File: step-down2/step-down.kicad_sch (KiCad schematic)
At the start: 22 parts, among them IC1 LTC3807EFE#PBF, IC2 IRF7413ZPBF, IC3 IRF7413ZPBF, J1 Screw_Terminal_01x02, J2 Screw_Terminal_01x02

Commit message: fixed mosfet connections
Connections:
- net GND: now also IC3.2 (S_2), IC3.3 (S_3)
- net at C5.2, D2.1 (K), IC1.13 (SW)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: now also IC2.2 (S_2), IC2.3 (S_3)
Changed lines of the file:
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@@
+	)
+	(junction
+		(at 203.2 90.17)
+		(diameter 0)
+		(color 0 0 0 0)
 	)
 	(junction
@@
 	)
 	(junction
+		(at 203.2 92.71)
+		(diameter 0)
+		(color 0 0 0 0)
+	)
+	(junction
+		(at 203.2 71.12)
+		(diameter 0)
+		(color 0 0 0 0)
+	)
+	(junction
 		(at 231.14 110.49)
 		(diameter 0)
@@
 	(junction
 		(at 163.83 82.55)
+		(diameter 0)
+		(color 0 0 0 0)
+	)
+	(junction
+		(at 203.2 68.58)
 		(diameter 0)
 		(color 0 0 0 0)
@@
 	(wire
 		(pts
+			(xy 203.2 90.17) (xy 203.2 92.71)
+		)
+		(stroke
+			(width 0)
+			(type default)
+		)
+	)
+	(wire
+		(pts
 			(xy 233.68 97.79) (xy 233.68 101.6)
 		)
@@
 		)
 		(stroke
+			(width 0)
+			(type default)
+		)
+	)
+	(wire
+		(pts
+			(xy 203.2 68.58) (xy 203.2 71.12)
+		)
+		(stroke

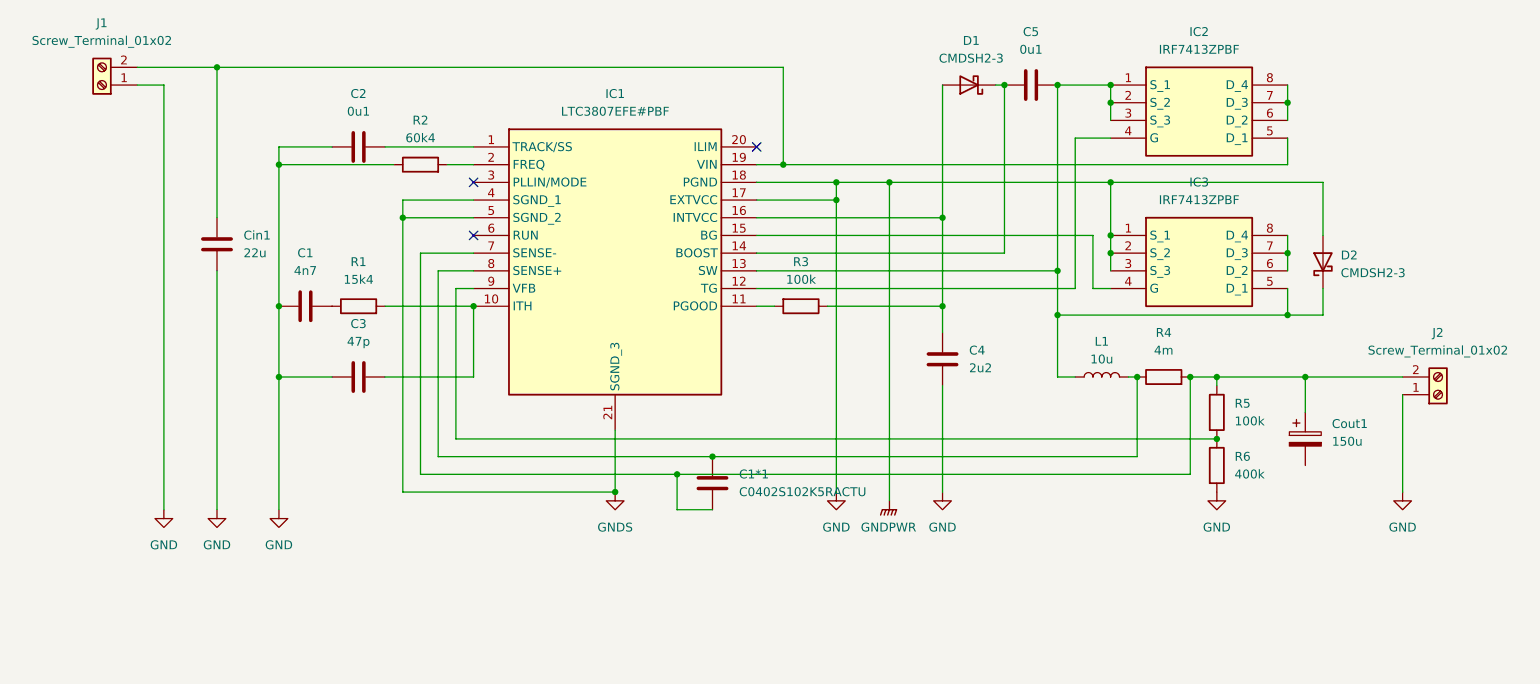
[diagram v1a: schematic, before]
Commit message: fixed mosfet connections
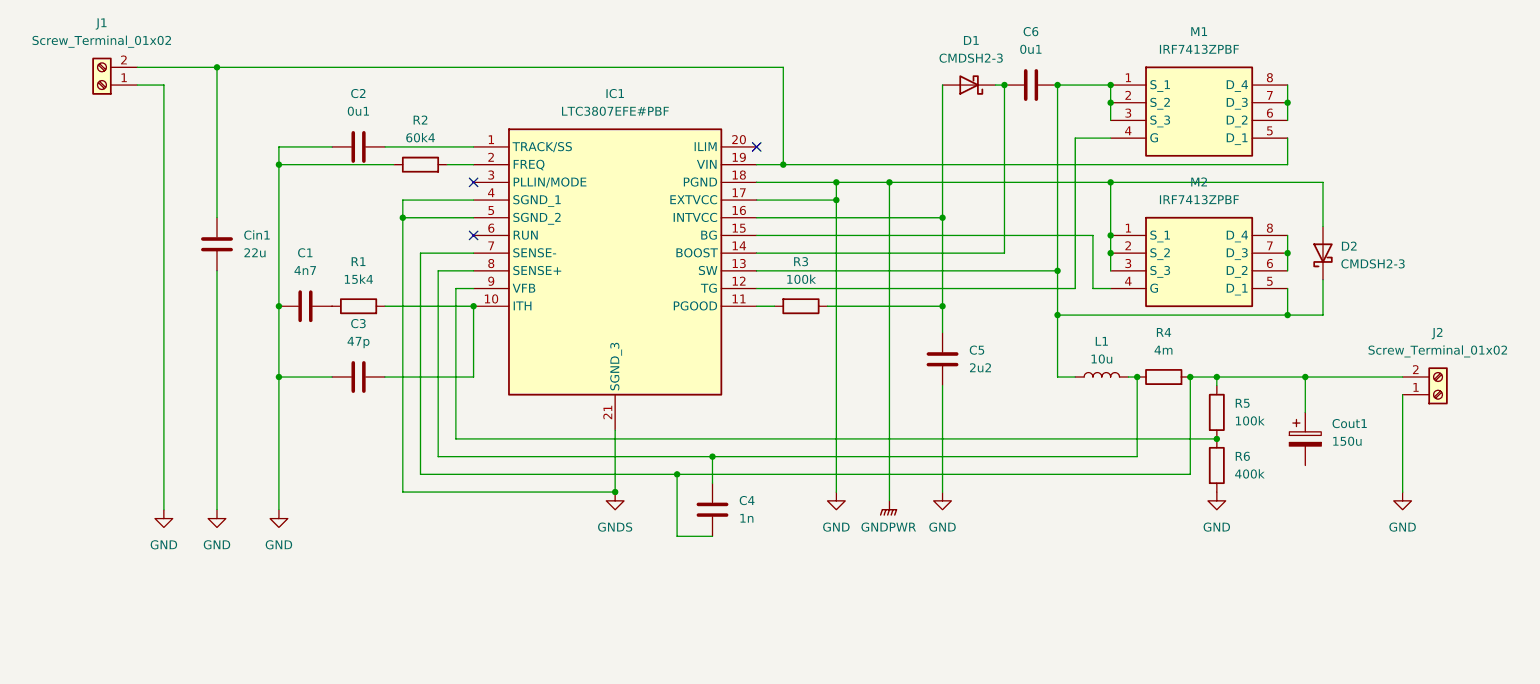
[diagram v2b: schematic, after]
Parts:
- C4: renamed from C1*1; value C0402S102K5RACTU -> 1n
- renumbered C4 to C5, C5 to C6, IC2 to M1, IC3 to M2
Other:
- moved on the sheet: C4, D2
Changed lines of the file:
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@@
 	(wire
 		(pts
-			(xy 140.97 124.46) (xy 140.97 129.54)
+			(xy 140.97 124.46) (xy 140.97 133.35)
 		)
 		(stroke
@@
 	(wire
 		(pts
-			(xy 233.68 82.55) (xy 233.68 90.17)
+			(xy 233.68 82.55) (xy 233.68 88.9)
 		)
 		(stroke
@@
 	(wire
 		(pts
+			(xy 146.05 125.73) (xy 146.05 121.92)
+		)
+		(stroke
+			(width 0)
+			(type default)
+		)
+	)
+	(wire
+		(pts
 			(xy 203.2 82.55) (xy 203.2 90.17)
 		)
@@
 	(wire
 		(pts
-			(xy 233.68 97.79) (xy 233.68 101.6)
+			(xy 233.68 96.52) (xy 233.68 101.6)
 		)
 		(stroke
@@
 	(wire
 		(pts
-			(xy 140.97 129.54) (xy 146.05 129.54)
+			(xy 140.97 133.35) (xy 146.05 133.35)
 		)
 		(stroke
@@
 	(symbol
 		(lib_id "Device:C")
-		(at 146.05 125.73 0)
+		(at 146.05 129.54 0)
 		(unit 1)
 		(exclude_from_sim no)
@@
 		(dnp no)
 		(fields_autoplaced yes)
-		(property "Reference" "C1*1"
-			(at 149.86 124.4599 0)
+		(property "Reference" "C4"
+			(at 149.86 128.2699 0)
 			(effects
 				(font
@@
 			)
 		)
-		(property "Value" "C0402S102K5RACTU"
-			(at 149.86 126.9999 0)
+		(property "Value" "1n"
+			(at 149.86 130.8099 0)
 			(effects
 				(font
@@
 		)
 		(property "Footprint" "C0402"
-			(at 147.0152 129.54 0)
+			(at 147.0152 133.35 0)
 			(effects
 				(font
@@
 		)
 		(property "Datasheet" "~"
-			(at 146.05 125.73 0)
+			(at 146.05 129.54 0)
 			(effects
 				(font
@@
 		)
 		(property "Description" "Unpolarized capacitor"
-			(at 146.05 125.73 0)
+			(at 146.05 129.54 0)
 			(effects
 				(font
@@
 		)
 		(property "Height" "0.55"
-			(at 154.94 521.92 0)
+			(at 154.94 525.73 0)
 			(effects
 				(font
@@
 		)
 		(property "Mouser Part Number" "80-C0402S102K5R"
-			(at 154.94 621.92 0)
+			(at 154.94 625.73 0)
 			(effects
 				(font
@@
 		)
 		(property "Mouser Price/Stock" "https://www.mouser.co.uk/ProductDetail/KEMET/C0402S102K5RACTU?qs=CV4an4nnCD1z917c3mAHAQ%3D%3D"
-			(at 154.94 721.92 0)
+			(at 154.94 725.73 0)
 			(effects
 				(font
@@
 		)
 		(property "Manufacturer_Name" "KEMET"
-			(at 154.94 821.92 0)
+			(at 154.94 825.73 0)
 			(effects
 				(font
@@
 		)
 		(property "Manufacturer_Part_Number" "C0402S102K5RACTU"
-			(at 154.94 921.92 0)
+			(at 154.94 925.73 0)
 			(effects
 				(font
@@
 			(project "step-down"
 				(path "/270a0c1d-99e0-47c8-a788-488ffbf33d34"
-					(reference "C1*1")
+					(reference "C4")
 					(unit 1)
 				)
@@
 		(dnp no)
 		(fields_autoplaced yes)
-		(property "Reference" "IC3"
+		(property "Reference" "M2"
 			(at 215.9 82.55 0)
 			(effects
@@
 			(project "step-down"
 				(path "/270a0c1d-99e0-47c8-a788-488ffbf33d34"
-					(reference "IC3")
+					(reference "M2")
 					(unit 1)
 				)
@@
 		(dnp no)
 		(fields_autoplaced yes)
-		(property "Reference" "C5"
+		(property "Reference" "C6"
 			(at 191.77 60.96 90)
 			(effects
@@
 			(project ""
 				(path "/270a0c1d-99e0-47c8-a788-488ffbf33d34"
-					(reference "C5")
+					(reference "C6")
 					(unit 1)
 				)
@@
 		(dnp no)
 		(fields_autoplaced yes)
-		(property "Reference" "IC2"
+		(property "Reference" "M1"
 			(at 215.9 60.96 0)
 			(effects
@@
 			(project ""
 				(path "/270a0c1d-99e0-47c8-a788-488ffbf33d34"
-					(reference "IC2")
+					(reference "M1")
 					(unit 1)
 				)
@@
 	(symbol
 		(lib_id "Device:D_Schottky")
-		(at 233.68 93.98 90)
+		(at 233.68 92.71 90)
 		(unit 1)
 		(exclude_from_sim no)
@@
 		(fields_autoplaced yes)
 		(property "Reference" "D2"
-			(at 236.22 93.0274 90)
+			(at 236.22 91.7574 90)
 			(effects
 				(font
@@
 		)
 		(property "Value" "CMDSH2-3"
-			(at 236.22 95.5674 90)
+			(at 236.22 94.2974 90)
 			(effects
 				(font
@@
 		)
 		(property "Footprint" "footprints:CMDSH2-3_TR_PBFREE"
-			(at 233.68 93.98 0)
+			(at 233.68 92.71 0)
 			(effects
 				(font
@@
 		)
 		(property "Datasheet" "~"
-			(at 233.68 93.98 0)
+			(at 233.68 92.71 0)
 			(effects
 				(font
@@
 		)
 		(property "Description" "Schottky diode"
-			(at 233.68 93.98 0)
+			(at 233.68 92.71 0)
 			(effects
 				(font
@@
 		(dnp no)
 		(fields_autoplaced yes)
-		(property "Reference" "C4"
+		(property "Reference" "C5"
 			(at 182.88 106.6799 0)
 			(effects
@@
 			(project ""
 				(path "/270a0c1d-99e0-47c8-a788-488ffbf33d34"
-					(reference "C4")
+					(reference "C5")
 					(unit 1)
 				)

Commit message: gnd fix
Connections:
- net GND: now also Cout1.2
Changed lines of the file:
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@@
+	(wire
+		(pts
+			(xy 231.14 123.19) (xy 231.14 127)
+		)
+		(stroke
+			(width 0)
+			(type default)
+		)
+	)
 	(wire
 		(pts
@@
 					(unit 1)
 				)
+			)
+		)
+	)
+	(symbol
+		(lib_id "power:GND")
+		(at 231.14 127 0)
+		(unit 1)
+		(exclude_from_sim no)
+		(in_bom yes)
+		(on_board yes)
+		(dnp no)
+		(fields_autoplaced yes)
+		(property "Reference" "#PWR010"
+			(at 231.14 133.35 0)
+			(effects
+				(font
+					(size 1.27 1.27)
+				)
+				(hide yes)
+			)
+		)
+		(property "Value" "GND"
+			(at 231.14 132.08 0)
+			(effects
+				(font
+					(size 1.27 1.27)
+				)
+			)
+		)
+		(property "Footprint" ""
+			(at 231.14 127 0)
+			(effects
+				(font
+					(size 1.27 1.27)
+				)
+				(hide yes)
+			)
+		)
+		(property "Datasheet" ""
+			(at 231.14 127 0)
+			(effects
+				(font
+					(size 1.27 1.27)
+				)
+				(hide yes)
+			)
+		)
+		(property "Description" "Power symbol creates a global label with name \"GND\" , ground"
+			(at 231.14 127 0)
+			(effects
+				(font
+					(size 1.27 1.27)
+				)
+				(hide yes)
+			)
+		)
+		(pin "1"
+		)
+		(instances
+			(project ""
+				(path "/270a0c1d-99e0-47c8-a788-488ffbf33d34"
+					(reference "#PWR010")
+					(unit 1)
+				)

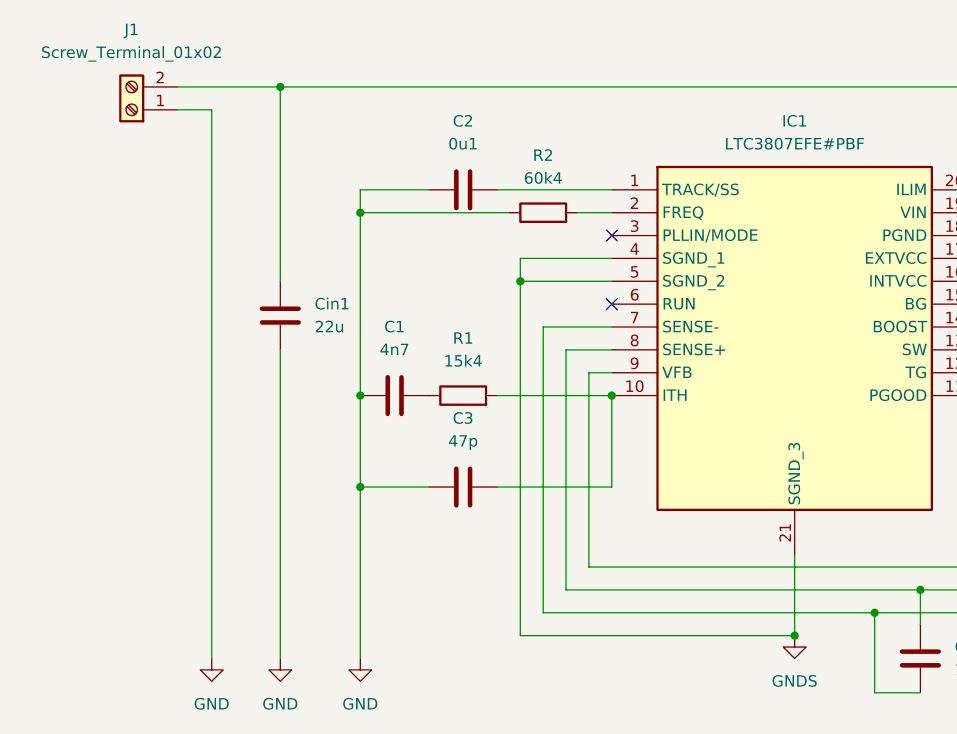
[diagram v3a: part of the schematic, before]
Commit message: fixed ERC error
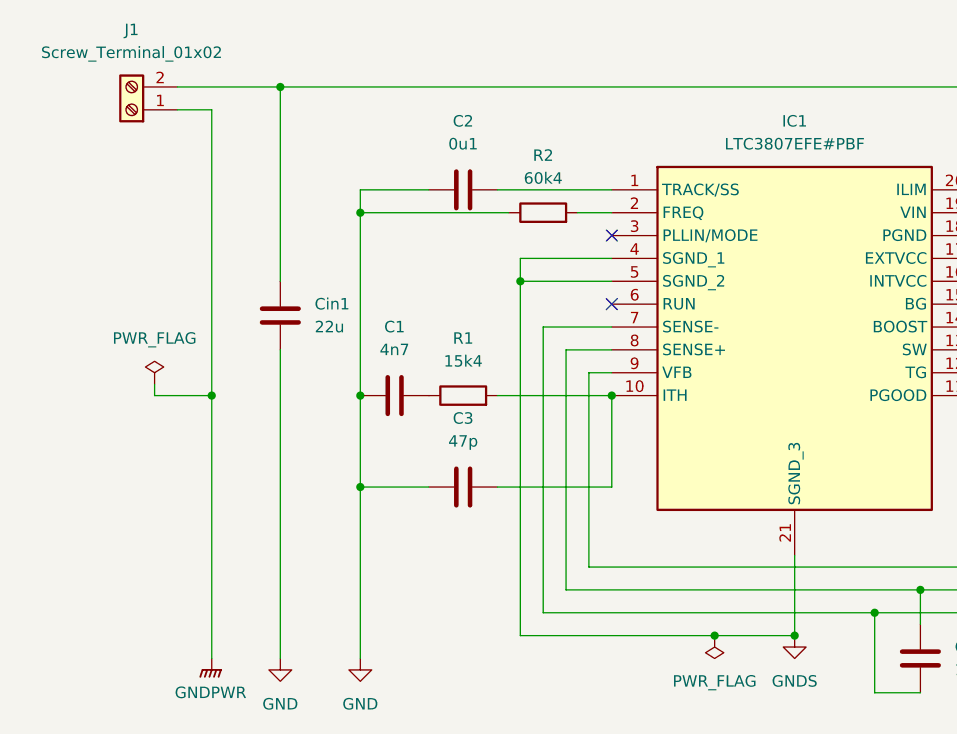
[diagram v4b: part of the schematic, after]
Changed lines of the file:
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@@
 	)
 	(junction
+		(at 67.31 100.33)
+		(diameter 0)
+		(color 0 0 0 0)
+	)
+	(junction
 		(at 179.07 100.33)
 		(diameter 0)
@@
 	)
 	(junction
+		(at 123.19 127)
+		(diameter 0)
+		(color 0 0 0 0)
+	)
+	(junction
 		(at 214.63 110.49)
 		(diameter 0)
@@
 	(wire
 		(pts
+			(xy 67.31 100.33) (xy 67.31 129.54)
+		)
+		(stroke
+			(width 0)
+			(type default)
+		)
+	)
+	(wire
+		(pts
 			(xy 187.96 68.58) (xy 187.96 92.71)
 		)
@@
 	(wire
 		(pts
-			(xy 101.6 127) (xy 132.08 127)
+			(xy 101.6 127) (xy 123.19 127)
 		)
 		(stroke
@@
 	(wire
 		(pts
+			(xy 123.19 127) (xy 132.08 127)
+		)
+		(stroke
+			(width 0)
+			(type default)
+		)
+	)
+	(wire
+		(pts
 			(xy 106.68 121.92) (xy 146.05 121.92)
 		)
@@
 	(wire
 		(pts
+			(xy 60.96 99.06) (xy 60.96 100.33)
+		)
+		(stroke
+			(width 0)
+			(type default)
+		)
+	)
+	(wire
+		(pts
 			(xy 179.07 87.63) (xy 179.07 100.33)
 		)
@@
 	(wire
 		(pts
-			(xy 67.31 68.58) (xy 67.31 129.54)
+			(xy 67.31 68.58) (xy 67.31 100.33)
 		)
 		(stroke
@@
 	(wire
 		(pts
+			(xy 60.96 100.33) (xy 67.31 100.33)
+		)
+		(stroke
+			(width 0)
+			(type default)
+		)
+	)
+	(wire
+		(pts
 			(xy 104.14 124.46) (xy 140.97 124.46)
 		)
@@
 	(symbol
 		(lib_id "power:GND")
-		(at 67.31 129.54 0)
+		(at 231.14 127 0)
 		(unit 1)
 		(exclude_from_sim no)
@@
 		(dnp no)
 		(fields_autoplaced yes)
-		(property "Reference" "#PWR01"
-			(at 67.31 135.89 0)
+		(property "Reference" "#PWR010"
+			(at 231.14 133.35 0)
 			(effects
 				(font
@@
 		)
 		(property "Value" "GND"
-			(at 67.31 134.62 0)
+			(at 231.14 132.08 0)
 			(effects
 				(font
@@
 		)
 		(property "Footprint" ""
-			(at 67.31 129.54 0)
+			(at 231.14 127 0)
 			(effects
 				(font
@@
 		)
 		(property "Datasheet" ""
-			(at 67.31 129.54 0)
+			(at 231.14 127 0)
 			(effects
 				(font
@@
 		)
 		(property "Description" "Power symbol creates a global label with name \"GND\" , ground"
-			(at 67.31 129.54 0)
+			(at 231.14 127 0)
 			(effects
 				(font
@@
 			(project ""
 				(path "/270a0c1d-99e0-47c8-a788-488ffbf33d34"
-					(reference "#PWR01")
+					(reference "#PWR010")
 					(unit 1)
 				)
@@
 	)
 	(symbol
-		(lib_id "power:GND")
-		(at 231.14 127 0)
+		(lib_id "Device:R")
+		(at 104.14 80.01 90)
 		(unit 1)
 		(exclude_from_sim no)
@@
 		(dnp no)
 		(fields_autoplaced yes)
-		(property "Reference" "#PWR010"
-			(at 231.14 133.35 0)
+		(property "Reference" "R2"
+			(at 104.14 73.66 90)
 			(effects
 				(font
 					(size 1.27 1.27)
 				)
-				(hide yes)
 			)
 		)
-		(property "Value" "GND"
-			(at 231.14 132.08 0)
+		(property "Value" "60k4"
+			(at 104.14 76.2 90)
 			(effects
 				(font
@@
 			)
 		)
-		(property "Footprint" ""
-			(at 231.14 127 0)
+		(property "Footprint" "footprints:ERJ-XGNF6042Y"
+			(at 104.14 81.788 90)
 			(effects
 				(font
@@
 			)
 		)
-		(property "Datasheet" ""
-			(at 231.14 127 0)
+		(property "Datasheet" "~"
+			(at 104.14 80.01 0)
 			(effects
 				(font
@@
 			)
 		)
-		(property "Description" "Power symbol creates a global label with name \"GND\" , ground"
-			(at 231.14 127 0)
+		(property "Description" "Resistor"
+			(at 104.14 80.01 0)
 			(effects
 				(font
@@
 		(pin "1"
 		)
+		(pin "2"
+		)
 		(instances
 			(project ""
 				(path "/270a0c1d-99e0-47c8-a788-488ffbf33d34"
-					(reference "#PWR010")
+					(reference "R2")
 					(unit 1)
 				)
@@
 	)
 	(symbol
-		(lib_id "Device:R")
-		(at 104.14 80.01 90)
+		(lib_id "power:PWR_FLAG")
+		(at 123.19 127 180)
 		(unit 1)
 		(exclude_from_sim no)
@@
 		(dnp no)
 		(fields_autoplaced yes)
-		(property "Reference" "R2"
-			(at 104.14 73.66 90)
+		(property "Reference" "#FLG02"
+			(at 123.19 128.905 0)
 			(effects
 				(font
 					(size 1.27 1.27)
 				)
+				(hide yes)
 			)
 		)
-		(property "Value" "60k4"
-			(at 104.14 76.2 90)
+		(property "Value" "PWR_FLAG"
+			(at 123.19 132.08 0)
 			(effects
 				(font
@@
 			)
 		)
-		(property "Footprint" "footprints:ERJ-XGNF6042Y"
-			(at 104.14 81.788 90)
+		(property "Footprint" ""
+			(at 123.19 127 0)
 			(effects
 				(font
@@
 		)
 		(property "Datasheet" "~"
-			(at 104.14 80.01 0)
+			(at 123.19 127 0)
 			(effects
 				(font
@@
 			)
 		)
-		(property "Description" "Resistor"
-			(at 104.14 80.01 0)
+		(property "Description" "Special symbol for telling ERC where power comes from"
+			(at 123.19 127 0)
 			(effects
 				(font
@@
 		(pin "1"
 		)
-		(pin "2"
-		)
 		(instances
 			(project ""
 				(path "/270a0c1d-99e0-47c8-a788-488ffbf33d34"
-					(reference "R2")
+					(reference "#FLG02")
 					(unit 1)
 				)
@@
 					(unit 1)
 				)
+			)
+		)
+	)
+	(symbol
+		(lib_id "power:PWR_FLAG")
+		(at 60.96 99.06 0)
+		(unit 1)
+		(exclude_from_sim no)
+		(in_bom yes)
+		(on_board yes)
+		(dnp no)
+		(fields_autoplaced yes)
+		(property "Reference" "#FLG01"
+			(at 60.96 97.155 0)
+			(effects
+				(font
+					(size 1.27 1.27)
+				)
+				(hide yes)
+			)
+		)
+		(property "Value" "PWR_FLAG"
+			(at 60.96 93.98 0)
+			(effects
+				(font
+					(size 1.27 1.27)
+				)
+			)
+		)
+		(property "Footprint" ""
+			(at 60.96 99.06 0)
+			(effects
+				(font
+					(size 1.27 1.27)
+				)
+				(hide yes)
+			)
+		)
+		(property "Datasheet" "~"
+			(at 60.96 99.06 0)
+			(effects
+				(font
+					(size 1.27 1.27)
+				)
+				(hide yes)
+			)
+		)
+		(property "Description" "Special symbol for telling ERC where power comes from"
+			(at 60.96 99.06 0)
+			(effects
+				(font
+					(size 1.27 1.27)
+				)
+				(hide yes)
+			)
+		)
+		(pin "1"
+		)
+		(instances
+			(project ""
+				(path "/270a0c1d-99e0-47c8-a788-488ffbf33d34"
+					(reference "#FLG01")
+					(unit 1)
+				)
+			)
+		)
+	)
+	(symbol
+		(lib_id "power:GNDPWR")
+		(at 67.31 129.54 0)
+		(unit 1)
+		(exclude_from_sim no)
+		(in_bom yes)
+		(on_board yes)
+		(dnp no)
+		(fields_autoplaced yes)
+		(property "Reference" "#PWR01"
+			(at 67.31 134.62 0)
+			(effects
+				(font
+					(size 1.27 1.27)
+				)
+				(hide yes)
+			)
+		)
+		(property "Value" "GNDPWR"
+			(at 67.183 133.35 0)
+			(effects
+				(font
+					(size 1.27 1.27)
+				)
+			)
+		)
+		(property "Footprint" ""
+			(at 67.31 130.81 0)
+			(effects
+				(font
+					(size 1.27 1.27)
+				)
+				(hide yes)
+			)
+		)
+		(property "Datasheet" ""
+			(at 67.31 130.81 0)
+			(effects
+				(font
+					(size 1.27 1.27)
+				)
+				(hide yes)
+			)
+		)
+		(property "Description" "Power symbol creates a global label with name \"GNDPWR\" , global ground"
+			(at 67.31 129.54 0)
+			(effects
+				(font
+					(size 1.27 1.27)
+				)
+				(hide yes)
+			)
+		)
+		(pin "1"
+		)
+		(instances
+			(project ""
+				(path "/270a0c1d-99e0-47c8-a788-488ffbf33d34"
+					(reference "#PWR01")
+					(unit 1)
+				)
